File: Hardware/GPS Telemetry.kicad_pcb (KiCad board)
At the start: 2 copper layers, 68 parts, among them J1 Micro_SD_Card_Det, J2 SWD, J3 Serial, J4 Conn_Coaxial, J5 USB_B_Micro, J6 Conn_01x02, J7 Screw_Terminal_01x02, SW1 BOOT, SW2 RST, U1 STM32F103C8Tx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

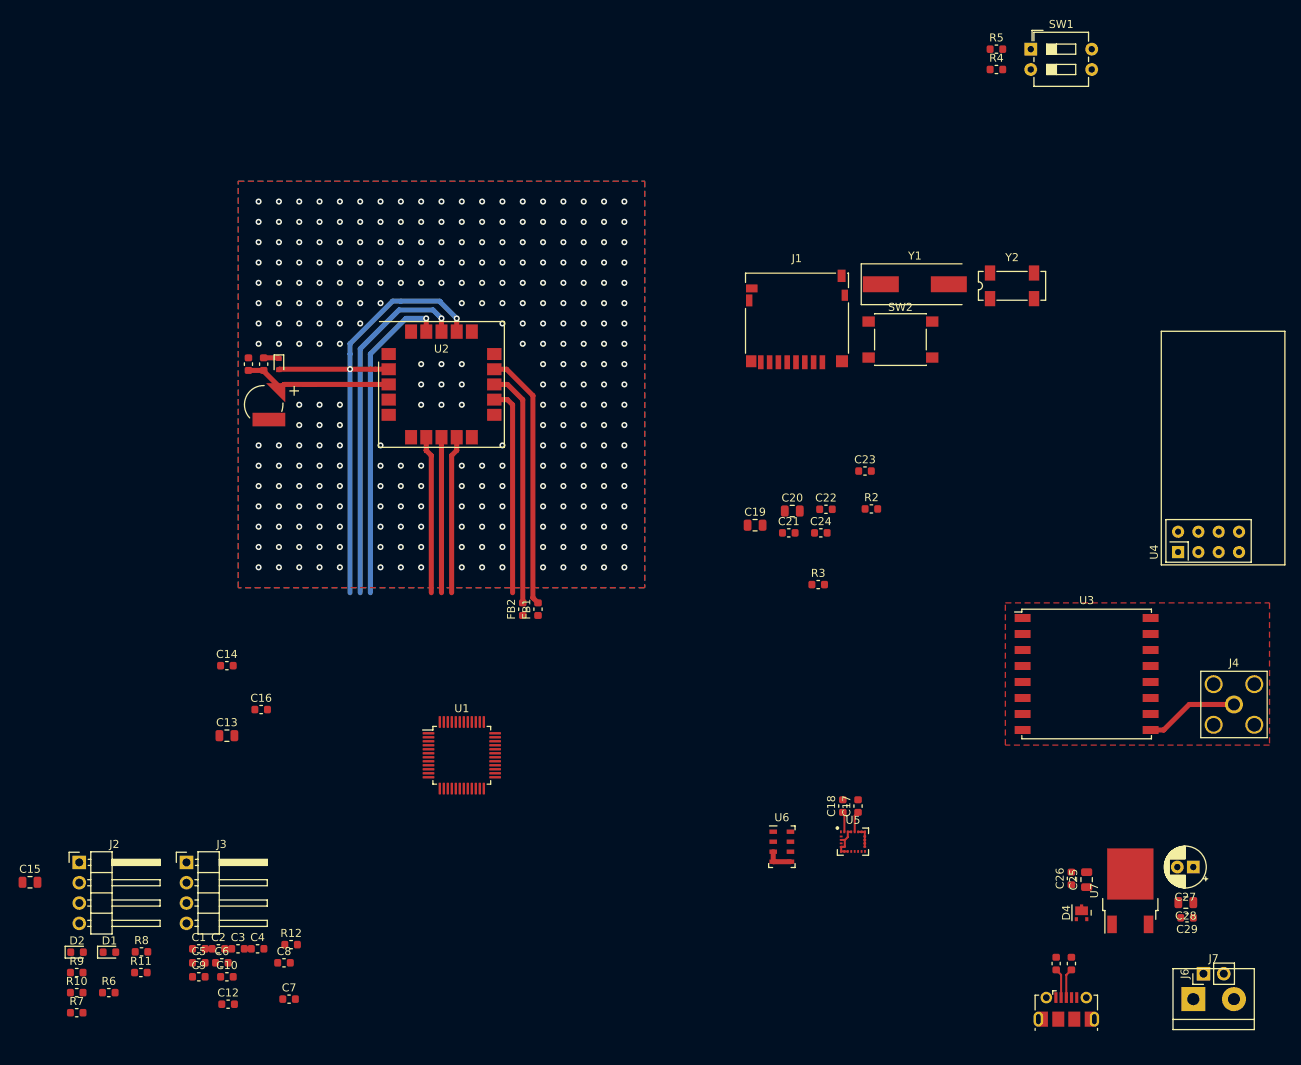
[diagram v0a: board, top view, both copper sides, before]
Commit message: Changed some footprints
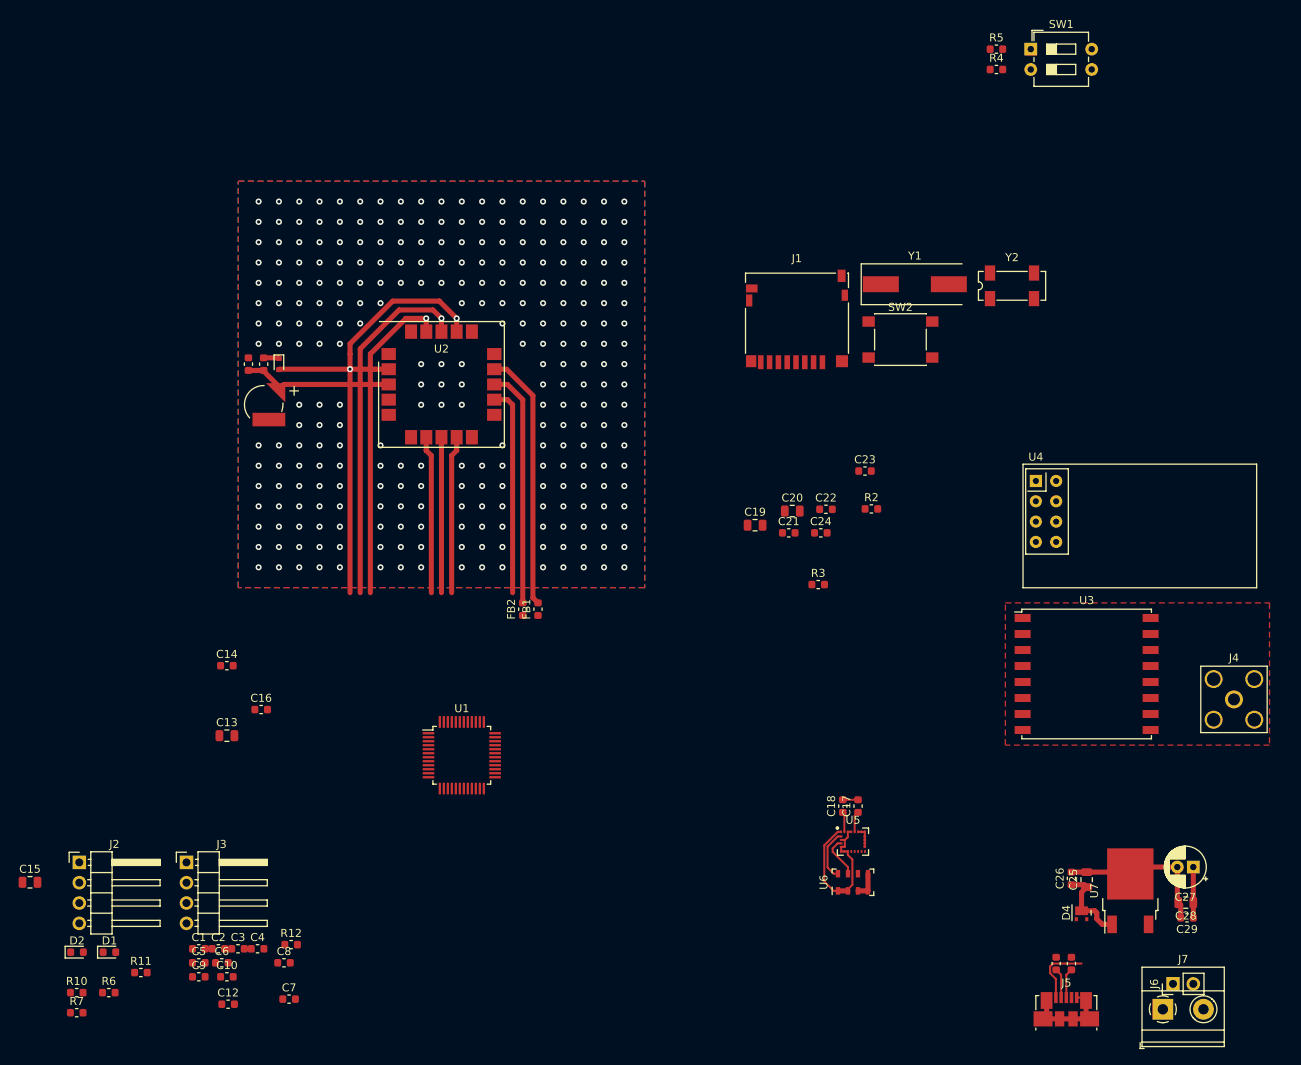
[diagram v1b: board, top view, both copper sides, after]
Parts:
- removed R8, R9: 22, Resistor_SMD:R_0603_1608Metric
- J5: footprint Connector_USB:USB_Micro-B_Molex-105017-0001 -> Connector_USB:USB_Micro-B_Molex_47346-0001
- J7: footprint TerminalBlock:TerminalBlock_bornier-2_P5.08mm -> TerminalBlock_Phoenix:TerminalBlock_Phoenix_MKDS-1,5-2-5.08_1x02_P5.08mm_Horizontal
- moved U4 19.9 mm to (229.2, 88.3), turned to 0 degrees
- moved U6 9.94 mm to (206.4, 138.4), turned to 90 degrees
- moved J6 4.02 mm to (246.4, 151.1)
- moved J7 4.02 mm to (245.1, 154.3)
- moved J4 0.64 mm to (254.0, 115.6)
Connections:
- U1 pad 30: /Microcontroller/TX -> /Microcontroller/A9
- U1 pad 31: /Microcontroller/RX -> /Microcontroller/A10
- U1 pad 32: Net-(R8-Pad2) -> /IO/POWER/USB_DM
- U1 pad 33: Net-(R9-Pad2) -> /IO/POWER/USB_DP
- U1 pad 42: /Microcontroller/B6 -> /Microcontroller/TX
- U1 pad 43: /Microcontroller/B7 -> /Microcontroller/RX
- U5 pad 10: /Microcontroller/B6 -> /Microcontroller/B10
- U5 pad 11: /Microcontroller/B7 -> /Microcontroller/B11
- U5 pad 12: /Microcontroller/B10 -> /Microcontroller/A9
- U5 pad 13: /Microcontroller/B11 -> /Microcontroller/A10
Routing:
- net GND: track 6.14 -> 40.4 mm
- net +3V3: track 67.8 -> 90.3 mm
- net Net-(J4-Pad1): track 11.7 -> 0.00 mm
- net Net-(C25-Pad1): track 0.00 -> 10.2 mm
- net VBUS: track 0.00 -> 8.27 mm
- net /Microcontroller/SCL: track 26.1 -> 32.5 mm
- net /Microcontroller/SDA: track 19.7 -> 25.0 mm
